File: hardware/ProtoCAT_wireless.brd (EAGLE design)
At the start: 59.7 x 53.3 mm, 70 parts, among them Q1 MOSFET-NCHANNELSMD, Q2 MOSFET-NCHANNELSMD, U1 ARDUINO, U3 TB6612FNG

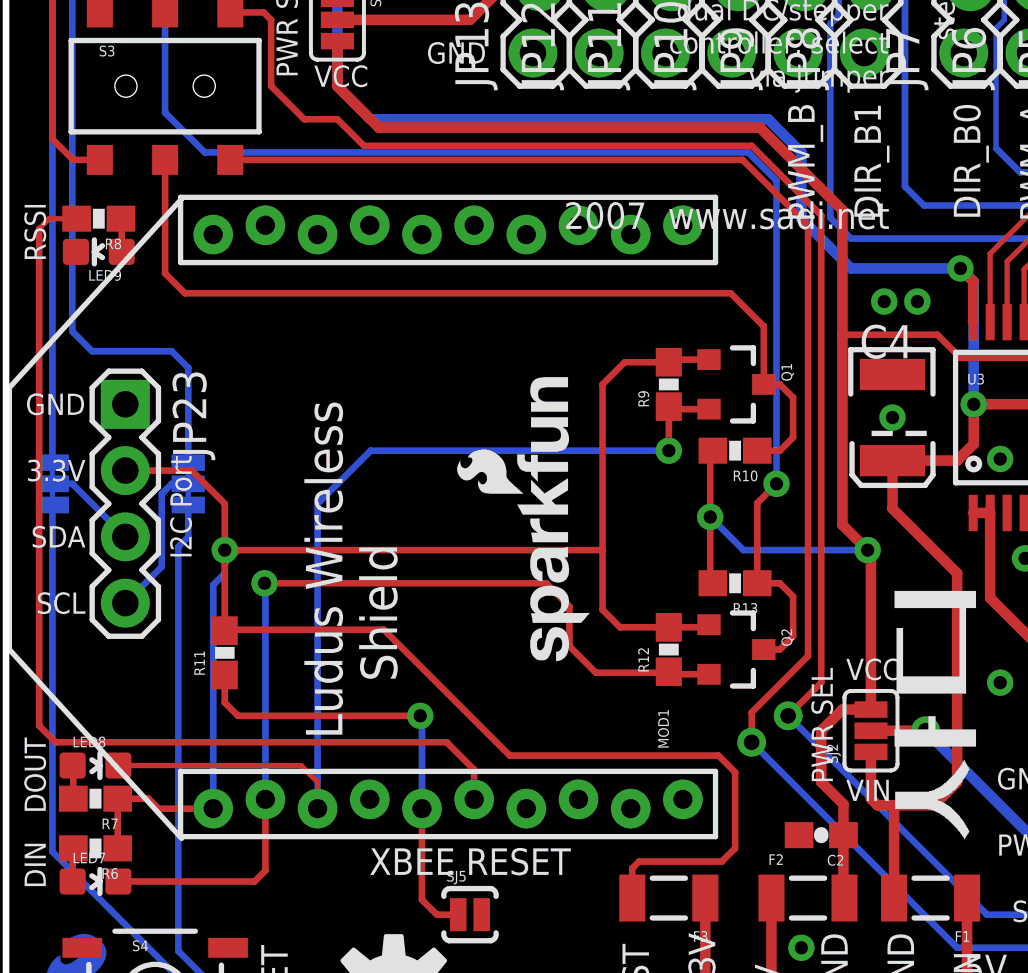
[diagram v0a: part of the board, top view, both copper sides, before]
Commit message: Added break-out for 4 I/O pins on XBee
Added breakout pins for DIO0, DIO1, P0, P1 and GND to the board.
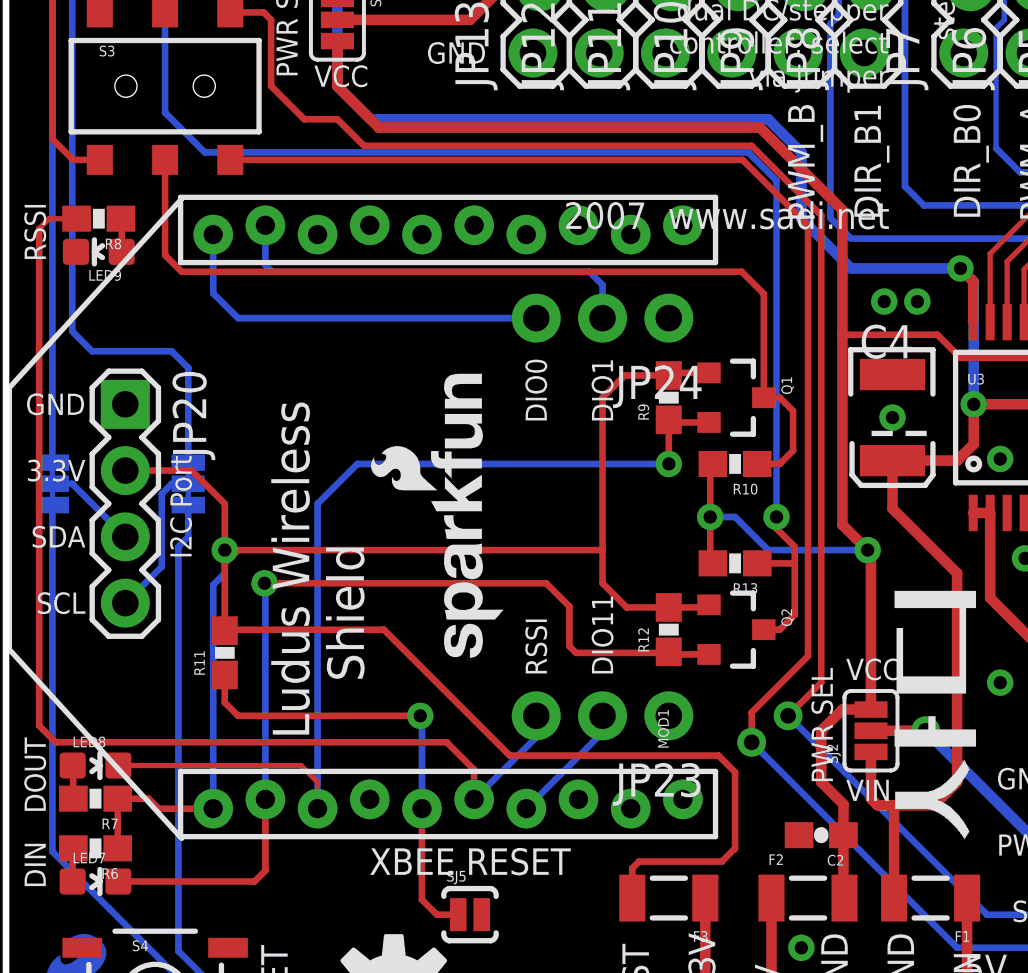
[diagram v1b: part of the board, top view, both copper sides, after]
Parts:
- added JP20: (no value), SparkFun-Connectors:1X04
- added JP24: (no value), SparkFun-Connectors:1X03_NO_SILK
- JP23: device SparkFun-Connectors:1X04 -> SparkFun-Connectors:1X03_NO_SILK
- moved JP23 24.0 mm to (25.4, 15.2), turned to 180 degrees
- moved LOGO2 3.30 mm to (19.2, 17.0)
- moved LOGO4 2.84 mm to (19.3, 27.6)
- moved Q2 0.76 mm to (27.9, 18.5)
- moved R12 0.76 mm to (25.4, 18.5)
- moved R13 0.76 mm to (27.9, 21.1)
- moved Q1 0.51 mm to (27.9, 27.4)
- moved R9 0.51 mm to (25.4, 27.4)
- moved R10 0.51 mm to (27.9, 24.9)
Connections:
- new net DIO0: JP24.3, MOD1.20
- new net DIO1: JP24.2, MOD1.19
- new net DIO11: JP23.2, MOD1.7
- net FUSED_3.3V: now also JP20.2; no longer JP23.2
- net GND: now also JP20.1, JP24.1
- net RSSI: now also JP23.3
- net SCL_I2C_PORT: now also JP20.4; no longer JP23.4
- net SDA_I2C_PORT: now also JP20.3; no longer JP23.3
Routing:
- net DIO1: track 0.00 -> 16.0 mm
- net DIO0: track 0.00 -> 15.0 mm
- net DIO11: track 0.00 -> 4.77 mm
- net RSSI: track 39.1 -> 43.3 mm
- net FUSED_3.3V: track 87.4 -> 85.9 mm
- net FUSED_5V: track 76.8 -> 75.5 mm
- net XBEE_TXO: track 34.8 -> 35.6 mm
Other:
- board text added: "DIO0"
- board text added: "DIO1"
- board text added: "DIO11"
